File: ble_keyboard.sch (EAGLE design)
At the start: 23 parts, among them Q1 DMG6968U-7, Q2 DMG2305UX-7, U1 YJ-14015

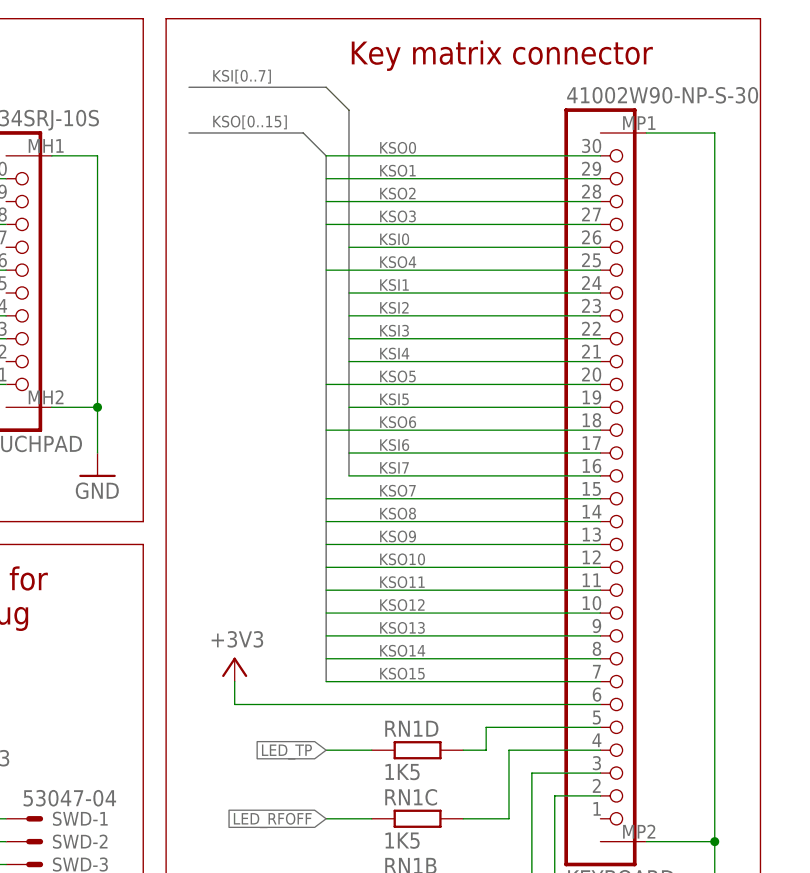
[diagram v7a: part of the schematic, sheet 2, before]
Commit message: - Fix P ch FET footprint - Add a note about unconnected LEDs
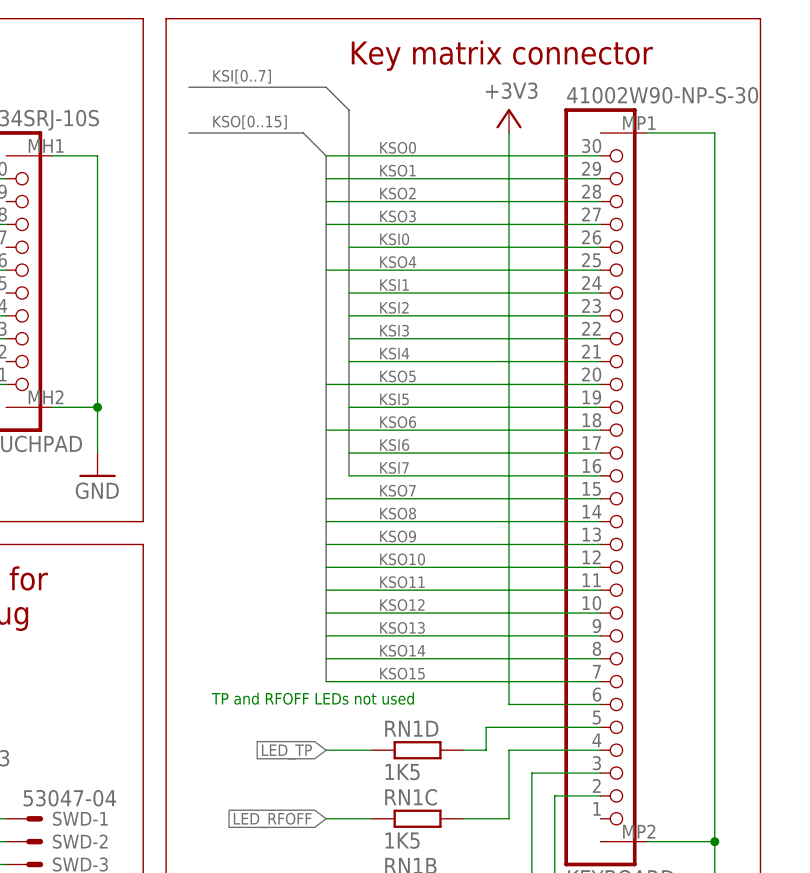
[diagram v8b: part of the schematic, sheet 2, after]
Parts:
- Q2: device transistor-fet:BSA223SP -> transistor-fet:BSA223SPSOT23
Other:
- note added: "TP and RFOFF LEDs not used"
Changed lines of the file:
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@@
 <grid distance="0.1" unitdist="inch" unit="inch" style="lines" multiple="1" display="no" altdistance="0.01" altunitdist="inch" altunit="inch"/>
 <layers>
-<layer number="1" name="Top" color="4" fill="1" visible="no" active="no"/>
-<layer number="2" name="Route2" color="1" fill="3" visible="no" active="no"/>
-<layer number="3" name="Route3" color="4" fill="3" visible="no" active="no"/>
-<layer number="4" name="Route4" color="1" fill="4" visible="no" active="no"/>
-<layer number="5" name="Route5" color="4" fill="4" visible="no" active="no"/>
-<layer number="6" name="Route6" color="1" fill="8" visible="no" active="no"/>
-<layer number="7" name="Route7" color="4" fill="8" visible="no" active="no"/>
-<layer number="8" name="Route8" color="1" fill="2" visible="no" active="no"/>
-<layer number="9" name="Route9" color="4" fill="2" visible="no" active="no"/>
-<layer number="10" name="Route10" color="1" fill="7" visible="no" active="no"/>
-<layer number="11" name="Route11" color="4" fill="7" visible="no" active="no"/>
-<layer number="12" name="Route12" color="1" fill="5" visible="no" active="no"/>
-<layer number="13" name="Route13" color="4" fill="5" visible="no" active="no"/>
-<layer number="14" name="Route14" color="1" fill="6" visible="no" active="no"/>
-<layer number="15" name="Route15" color="4" fill="6" visible="no" active="no"/>
-<layer number="16" name="Bottom" color="1" fill="1" visible="no" active="no"/>
-<layer number="17" name="Pads" color="2" fill="1" visible="no" active="no"/>
-<layer number="18" name="Vias" color="2" fill="1" visible="no" active="no"/>
-<layer number="19" name="Unrouted" color="6" fill="1" visible="no" active="no"/>
-<layer number="20" name="Dimension" color="15" fill="1" visible="no" active="no"/>
-<layer number="21" name="tPlace" color="7" fill="1" visible="no" active="no"/>
-<layer number="22" name="bPlace" color="7" fill="1" visible="no" active="no"/>
-<layer number="23" name="tOrigins" color="15" fill="1" visible="no" active="no"/>
-<layer number="24" name="bOrigins" color="15" fill="1" visible="no" active="no"/>
-<layer number="25" name="tNames" color="7" fill="1" visible="no" active="no"/>
-<layer number="26" name="bNames" color="7" fill="1" visible="no" active="no"/>
-<layer number="27" name="tValues" color="7" fill="1" visible="no" active="no"/>
-<layer number="28" name="bValues" color="7" fill="1" visible="no" active="no"/>
+<layer number="1" name="Top" color="4" fill="1" visible="yes" active="no"/>
+<layer number="2" name="Route2" color="1" fill="3" visible="yes" active="no"/>
+<layer number="3" name="Route3" color="4" fill="3" visible="yes" active="no"/>
+<layer number="4" name="Route4" color="1" fill="4" visible="yes" active="no"/>
+<layer number="5" name="Route5" color="4" fill="4" visible="yes" active="no"/>
+<layer number="6" name="Route6" color="1" fill="8" visible="yes" active="no"/>
+<layer number="7" name="Route7" color="4" fill="8" visible="yes" active="no"/>
+<layer number="8" name="Route8" color="1" fill="2" visible="yes" active="no"/>
+<layer number="9" name="Route9" color="4" fill="2" visible="yes" active="no"/>
+<layer number="10" name="Route10" color="1" fill="7" visible="yes" active="no"/>
+<layer number="11" name="Route11" color="4" fill="7" visible="yes" active="no"/>
+<layer number="12" name="Route12" color="1" fill="5" visible="yes" active="no"/>
+<layer number="13" name="Route13" color="4" fill="5" visible="yes" active="no"/>
+<layer number="14" name="Route14" color="1" fill="6" visible="yes" active="no"/>
+<layer number="15" name="Route15" color="4" fill="6" visible="yes" active="no"/>
+<layer number="16" name="Bottom" color="1" fill="1" visible="yes" active="no"/>
+<layer number="17" name="Pads" color="2" fill="1" visible="yes" active="no"/>
+<layer number="18" name="Vias" color="2" fill="1" visible="yes" active="no"/>
+<layer number="19" name="Unrouted" color="6" fill="1" visible="yes" active="no"/>
+<layer number="20" name="Dimension" color="15" fill="1" visible="yes" active="no"/>
+<layer number="21" name="tPlace" color="7" fill="1" visible="yes" active="no"/>
+<layer number="22" name="bPlace" color="7" fill="1" visible="yes" active="no"/>
+<layer number="23" name="tOrigins" color="15" fill="1" visible="yes" active="no"/>
+<layer number="24" name="bOrigins" color="15" fill="1" visible="yes" active="no"/>
+<layer number="25" name="tNames" color="7" fill="1" visible="yes" active="no"/>
+<layer number="26" name="bNames" color="7" fill="1" visible="yes" active="no"/>
+<layer number="27" name="tValues" color="7" fill="1" visible="yes" active="no"/>
+<layer number="28" name="bValues" color="7" fill="1" visible="yes" active="no"/>
 <layer number="29" name="tStop" color="7" fill="3" visible="no" active="no"/>
 <layer number="30" name="bStop" color="7" fill="6" visible="no" active="no"/>
@@
 <layer number="35" name="tGlue" color="7" fill="4" visible="no" active="no"/>
 <layer number="36" name="bGlue" color="7" fill="5" visible="no" active="no"/>
-<layer number="37" name="tTest" color="7" fill="1" visible="no" active="no"/>
-<layer number="38" name="bTest" color="7" fill="1" visible="no" active="no"/>
+<layer number="37" name="tTest" color="7" fill="1" visible="yes" active="no"/>
+<layer number="38" name="bTest" color="7" fill="1" visible="yes" active="no"/>
 <layer number="39" name="tKeepout" color="4" fill="11" visible="no" active="no"/>
 <layer number="40" name="bKeepout" color="1" fill="11" visible="no" active="no"/>
@@
 <layer number="44" name="Drills" color="7" fill="1" visible="no" active="no"/>
 <layer number="45" name="Holes" color="7" fill="1" visible="no" active="no"/>
-<layer number="46" name="Milling" color="3" fill="1" visible="no" active="no"/>
-<layer number="47" name="Measures" color="7" fill="1" visible="no" active="no"/>
-<layer number="48" name="Document" color="7" fill="1" visible="no" active="no"/>
-<layer number="49" name="Reference" color="7" fill="1" visible="no" active="no"/>
-<layer number="50" name="dxf" color="7" fill="1" visible="no" active="no"/>
-<layer number="51" name="tDocu" color="7" fill="1" visible="no" active="no"/>
-<layer number="52" name="bDocu" color="7" fill="1" visible="no" active="no"/>
-<layer number="53" name="tGND_GNDA" color="7" fill="9" visible="no" active="no"/>
-<layer number="54" name="bGND_GNDA" color="1" fill="9" visible="no" active="no"/>
-<layer number="56" name="wert" color="7" fill="1" visible="no" active="no"/>
-<layer number="57" name="tCAD" color="7" fill="1" visible="no" active="no"/>
-<layer number="59" name="tCarbon" color="7" fill="1" visible="no" active="no"/>
-<layer number="60" name="bCarbon" color="7" fill="1" visible="no" active="no"/>
-<layer number="61" name="stand" color="7" fill="1" visible="no" active="no"/>
+<layer number="46" name="Milling" color="3" fill="1" visible="yes" active="no"/>
+<layer number="47" name="Measures" color="7" fill="1" visible="yes" active="no"/>
+<layer number="48" name="Document" color="7" fill="1" visible="yes" active="no"/>
+<layer number="49" name="Reference" color="7" fill="1" visible="yes" active="no"/>
+<layer number="50" name="dxf" color="7" fill="1" visible="yes" active="no"/>
+<layer number="51" name="tDocu" color="7" fill="1" visible="yes" active="no"/>
+<layer number="52" name="bDocu" color="7" fill="1" visible="yes" active="no"/>
+<layer number="53" name="tGND_GNDA" color="7" fill="9" visible="yes" active="no"/>
+<layer number="54" name="bGND_GNDA" color="1" fill="9" visible="yes" active="no"/>
+<layer number="56" name="wert" color="7" fill="1" visible="yes" active="no"/>
+<layer number="57" name="tCAD" color="7" fill="1" visible="yes" active="no"/>
+<layer number="59" name="tCarbon" color="7" fill="1" visible="yes" active="no"/>
+<layer number="60" name="bCarbon" color="7" fill="1" visible="yes" active="no"/>
+<layer number="61" name="stand" color="7" fill="1" visible="yes" active="no"/>
 <layer number="90" name="Modules" color="5" fill="1" visible="yes" active="yes"/>
 <layer number="91" name="Nets" color="2" fill="1" visible="yes" active="yes"/>
@@
 <part name="KEYBOARD" library="JTC41002" deviceset="41002W90-NP-S-30" device=""/>
 <part name="+3V8" library="supply1" deviceset="+3V3" device=""/>
-<part name="Q2" library="transistor-fet" deviceset="BSA223SP" device="" value="DMG2305UX-7">
+<part name="Q2" library="transistor-fet" deviceset="BSA223SP" device="SOT23" value="DMG2305UX-7">
 <attribute name="OC_TME" value="DMG2305UX-7"/>
 </part>
@@
 <wire x1="5.08" y1="5.08" x2="5.08" y2="33.02" width="0.1524" layer="94"/>
 <text x="7.62" y="30.48" size="2.54" layer="94" font="vector" align="top-left">KBD backlight driver</text>
+<text x="193.04" y="96.52" size="1.27" layer="91" font="vector">TP and RFOFF LEDs not used</text>
 </plain>
 <instances>
@@
 </instance>
 <instance part="+3V3" gate="G$1" x="167.64" y="88.9"/>
-<instance part="+3V4" gate="G$1" x="195.58" y="101.6" smashed="yes">
-<attribute name="VALUE" x="192.786" y="102.87" size="1.778" layer="96"/>
+<instance part="+3V4" gate="G$1" x="226.06" y="162.56" smashed="yes">
+<attribute name="VALUE" x="223.266" y="163.83" size="1.778" layer="96"/>
 </instance>
 <instance part="VREG1" gate="VREG" x="66.04" y="154.94">
@@
 </segment>
 <segment>
-<wire x1="195.58" y1="99.06" x2="195.58" y2="96.52" width="0.1524" layer="91"/>
-<wire x1="195.58" y1="96.52" x2="236.22" y2="96.52" width="0.1524" layer="91"/>
+<wire x1="226.06" y1="160.02" x2="226.06" y2="96.52" width="0.1524" layer="91"/>
+<wire x1="226.06" y1="96.52" x2="236.22" y2="96.52" width="0.1524" layer="91"/>
 <pinref part="+3V4" gate="G$1" pin="+3V3"/>
 <pinref part="KEYBOARD" gate="G1" pin="6"/>
